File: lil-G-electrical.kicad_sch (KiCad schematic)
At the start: 34 parts, among them J101 XT-60, J102 XT-60, J103 GPIO, Q101 STD26P3LLH6, SW101 PVA1EE, U101 MCP1415, U102 TPS565208

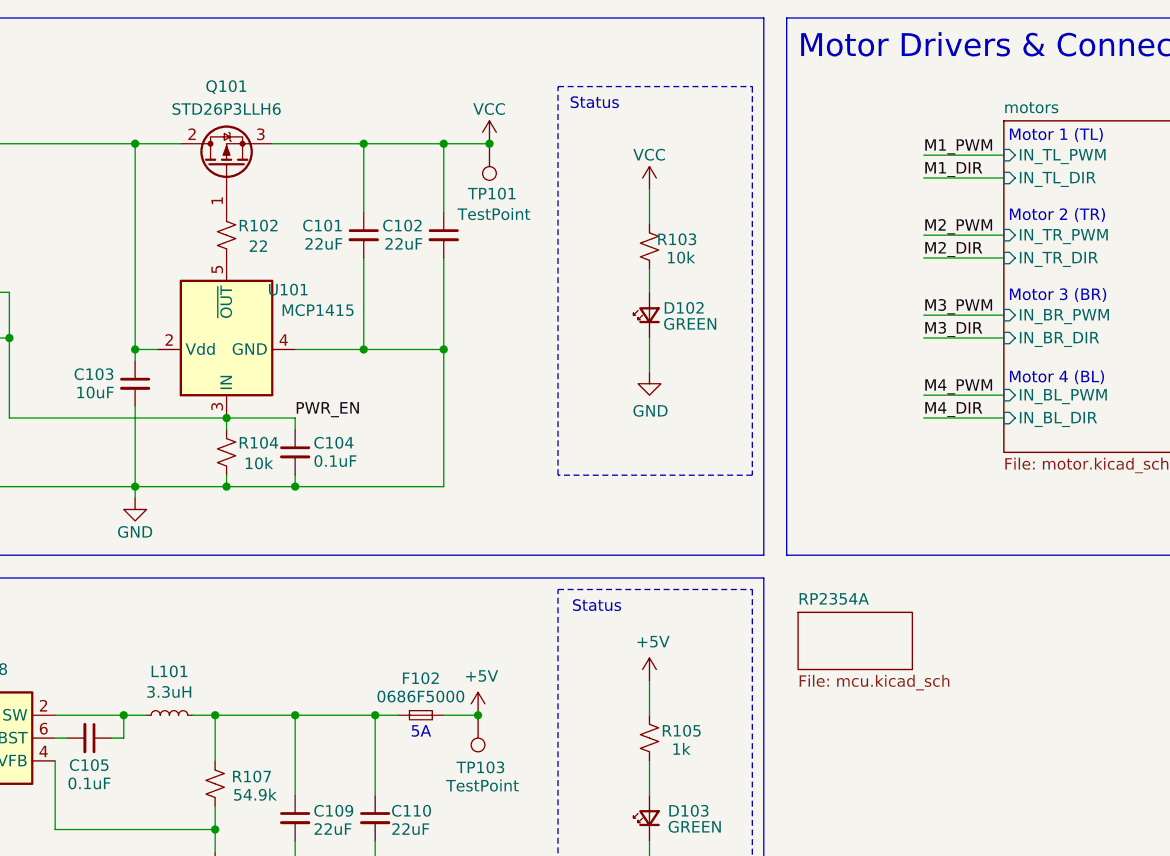
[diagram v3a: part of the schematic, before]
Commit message: fixed high-side power enable circuit. flipped PMOS source/drain
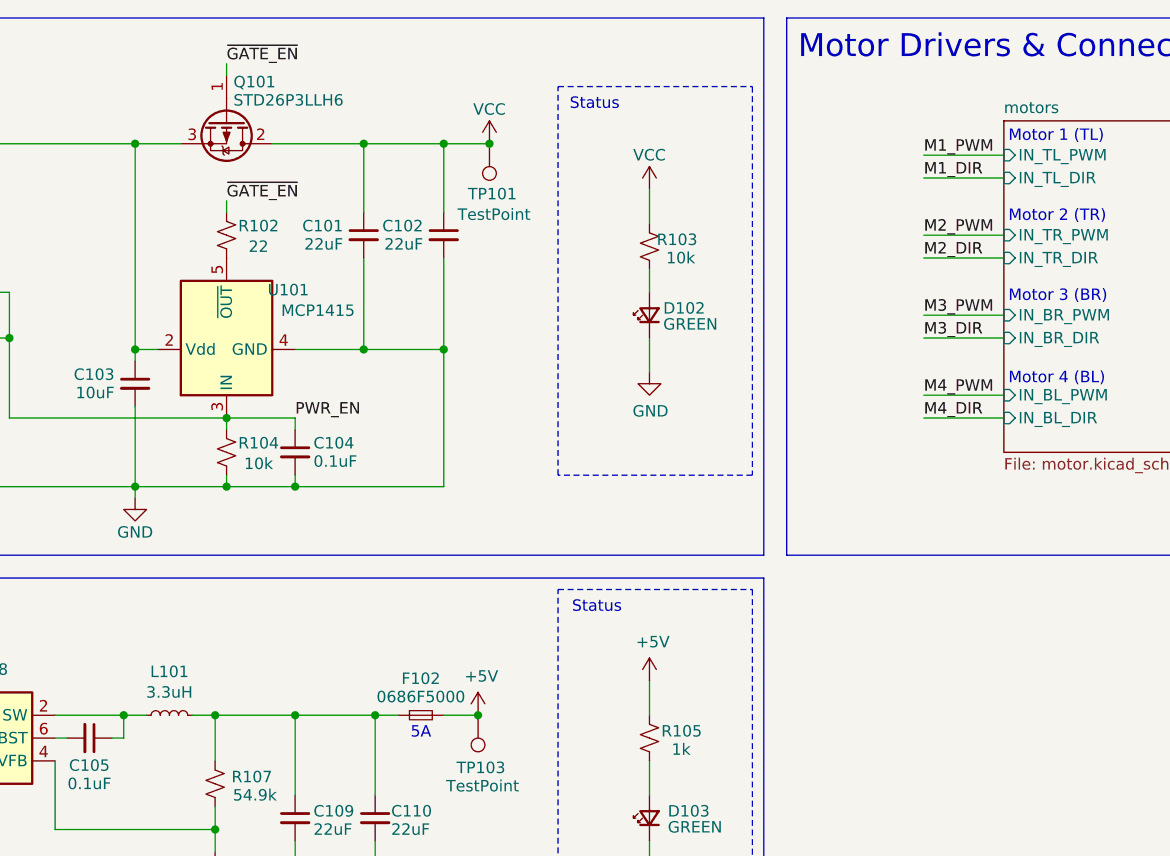
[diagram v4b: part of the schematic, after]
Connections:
- net VCC: now also Q101.2 (D); no longer Q101.3 (S)
- net at C103.1, F101.2, R101.1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: now also Q101.3 (S); no longer Q101.2 (D)
- net ~{GATE_EN}: now reaches Q101.1 (G), R102.1
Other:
- removed sheet RP2354A
- moved on the sheet: Q101
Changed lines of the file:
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@@
 	(wire
 		(pts
+			(xy 97.79 34.29) (xy 97.79 35.56)
+		)
+		(stroke
+			(width 0)
+			(type default)
+		)
+	)
+	(wire
+		(pts
 			(xy 68.58 144.78) (xy 93.98 144.78)
 		)
@@
 	(wire
 		(pts
+			(xy 97.79 19.05) (xy 97.79 20.32)
+		)
+		(stroke
+			(width 0)
+			(type default)
+		)
+	)
+	(wire
+		(pts
 			(xy 175.26 49.53) (xy 184.15 49.53)
 		)
@@
 		)
 	)
+	(label "~{GATE_EN}"
+		(at 97.79 19.05 0)
+		(fields_autoplaced yes)
+		(effects
+			(font
+				(size 1.27 1.27)
+			)
+			(justify left bottom)
+		)
+	)
 	(label "M4_DIR"
 		(at 175.26 58.42 0)
@@
 		)
 	)
+	(label "~{GATE_EN}"
+		(at 97.79 34.29 0)
+		(fields_autoplaced yes)
+		(effects
+			(font
+				(size 1.27 1.27)
+			)
+			(justify left bottom)
+		)
+	)
 	(label "M4_PWM"
 		(at 175.26 55.88 0)
@@
 	(symbol
 		(lib_id "Device:Q_PMOS_GDS")
-		(at 97.79 30.48 90)
+		(at 97.79 25.4 270)
 		(unit 1)
 		(exclude_from_sim no)
@@
 		(on_board yes)
 		(dnp no)
-		(fields_autoplaced yes)
 		(property "Reference" "Q101"
-			(at 97.79 21.59 90)
+			(at 98.552 21.082 90)
 			(effects
 				(font
 					(size 1.27 1.27)
 				)
+				(justify left)
 			)
 		)
 		(property "Value" "STD26P3LLH6"
-			(at 97.79 24.13 90)
+			(at 98.552 23.114 90)
 			(effects
 				(font
 					(size 1.27 1.27)
 				)
+				(justify left)
 			)
 		)
 		(property "Footprint" "Package_TO_SOT_SMD:TO-252-2"
-			(at 95.25 25.4 0)
+			(at 100.33 30.48 0)
 			(effects
 				(font
@@
 		)
 		(property "Datasheet" "~"
-			(at 97.79 30.48 0)
+			(at 97.79 25.4 0)
 			(effects
 				(font
@@
 		)
 		(property "Description" "P-MOSFET transistor, gate/drain/source"
-			(at 97.79 30.48 0)
+			(at 97.79 25.4 0)
 			(effects
 				(font
@@
 				)
 			)
-		)
-	)
-	(sheet
-		(at 161.29 80.01)
-		(size 12.7 6.35)
-		(fields_autoplaced yes)
-		(stroke
-			(width 0.1524)
-			(type solid)
-		)
-		(fill
-			(color 0 0 0 0.0000)
-		)
-		(property "Sheetname" "RP2354A"
-			(at 161.29 79.2984 0)
-			(effects
-				(font
-					(size 1.27 1.27)
-				)
-				(justify left bottom)
-			)
-		)
-		(property "Sheetfile" "mcu.kicad_sch"
-			(at 161.29 86.9446 0)
-			(effects
-				(font
-					(size 1.27 1.27)
-				)
-				(justify left top)
-			)
-		)
-		(instances
-			(project "lil-G-electrical"
-				(path "/e63e39d7-6ac0-4ffd-8aa3-1841a4541b55"
-					(page "3")
-				)
-			)

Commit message: version 2 done
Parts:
- removed D103: GREEN, LED_SMD:LED_0603_1608Metric, symbol Device:LED_Small
- removed J103: GPIO, Connector_PinSocket_2.54mm:PinSocket_2x20_P2.54mm_Vertical, symbol Connector_Generic:Conn_02x20_Odd_Even
- removed R105: 1k, Resistor_SMD:R_0603_1608Metric, symbol Device:R_Small_US
- removed SW101: PVA1EE, Button_Switch_THT:SW_Push_2P1T_Toggle_CK_PVA1xxH4xxxxxxV2, symbol Switch:SW_DPST
- removed TP102: TestPoint, TestPoint:TestPoint_Keystone_5000-5004_Miniature, symbol Connector:TestPoint
- added C11, C12: 10uF, Capacitor_SMD:C_0603_1608Metric, symbol Device:C_Small
- added C13: 100n, Capacitor_SMD:C_0402_1005Metric, symbol Device:C_Small
- added D3, D8: KT-0805G, LED_SMD:LED_0805_2012Metric, symbol Device:LED_Small
- added D4, D5, D6, D7: KT-0603W, LED_SMD:LED_0603_1608Metric, symbol Device:LED_Small
- added F3: 0467001.NRHF, Fuse:Fuse_0603_1608Metric, symbol Device:Fuse_Small
- added J2: XT30-U-M, Connector_AMASS:AMASS_XT30U-M_1x02_P5.0mm_Vertical, symbol Connector_Generic:Conn_01x02
- added J4: BM04B-SRSS-TB, Connector_JST:JST_SH_BM04B-SRSS-TB_1x04-1MP_P1.00mm_Vertical, symbol Connector_Generic_MountingPin:Conn_01x04_MountingPin
- added J5: BM03B-SRSS-TB, Connector_JST:JST_SH_BM03B-SRSS-TB_1x03-1MP_P1.00mm_Vertical, symbol Connector_Generic_MountingPin:Conn_01x03_MountingPin
- added R10, R11, R12, R13, R5, R9: 1k, Resistor_SMD:R_0402_1005Metric, symbol Device:R_Small_US
- added R14: 300k, Resistor_SMD:R_0603_1608Metric, symbol Device:R_Small_US
- added R15: 100k, Resistor_SMD:R_0603_1608Metric, symbol Device:R_Small_US
- added SW1: 5.8 ZSGT, lilG_footprints:5.8_ZSGT, symbol swwitches:SW_DPDT
- added TP2, TP4, TP5, TP6: 5001, TestPoint:TestPoint_Keystone_5000-5004_Miniature, symbol Connector:TestPoint
- added U3: NCP1117ST33T3G, digikey-footprints:SOT-223, symbol dk_PMIC-Voltage-Regulators-Linear:NCP1117ST33T3G
- C4: renamed from C104; value 0.1uF -> 100n; footprint Capacitor_SMD:C_0603_1608Metric -> Capacitor_SMD:C_0402_1005Metric
- C5: renamed from C105; value 0.1uF -> 100n; footprint Capacitor_SMD:C_0603_1608Metric -> Capacitor_SMD:C_0402_1005Metric
- C8: renamed from C108; value 0.1uF -> 100n; footprint Capacitor_SMD:C_0603_1608Metric -> Capacitor_SMD:C_0402_1005Metric
- D1: renamed from D102; value GREEN -> KT-0805G; footprint LED_SMD:LED_0603_1608Metric -> LED_SMD:LED_0805_2012Metric
- F1: renamed from F101; value 01000065Z -> 01530007Z; footprint lilG_footprints:LittleFuse_Mini_100_SMD -> lilG_footprints:LittleFuse_01530007Z
- F2: renamed from F102; value 0686F5000 -> S0603-S-5.0A
- J1: renamed from J101; value XT-60 -> XT60-PW-M; footprint Connector_AMASS:AMASS_XT60-M_1x02_P7.20mm_Vertical -> Connector_AMASS:AMASS_XT60PW-M_1x02_P7.20mm_Horizontal; now in the parts list
- J3: renamed from J102; value XT-60 -> XT60-PW-M; footprint Connector_AMASS:AMASS_XT60-M_1x02_P7.20mm_Vertical -> Connector_AMASS:AMASS_XT60PW-M_1x02_P7.20mm_Horizontal; now in the parts list
- L1: renamed from L101; value 3.3uH -> SRP5030T-3R3M
- Q1: renamed from Q101; value STD26P3LLH6 -> 40P30
- R1: renamed from R101; footprint Resistor_SMD:R_0603_1608Metric -> Resistor_SMD:R_0402_1005Metric
- R2: renamed from R103; value 10k -> 4.7k; footprint Resistor_SMD:R_0603_1608Metric -> Resistor_SMD:R_0402_1005Metric
- R3: renamed from R102; footprint Resistor_SMD:R_0603_1608Metric -> Resistor_SMD:R_0402_1005Metric
- R4: renamed from R104; footprint Resistor_SMD:R_0603_1608Metric -> Resistor_SMD:R_0402_1005Metric
- R6: renamed from R106; footprint Resistor_SMD:R_0603_1608Metric -> Resistor_SMD:R_0402_1005Metric
- R7: renamed from R107; footprint Resistor_SMD:R_0603_1608Metric -> Resistor_SMD:R_0402_1005Metric
- R8: renamed from R108; footprint Resistor_SMD:R_0603_1608Metric -> Resistor_SMD:R_0402_1005Metric
- TP1: renamed from TP101; value TestPoint -> 5001
- TP3: renamed from TP103; value TestPoint -> 5001
- renumbered C101 to C1, C110 to C10, C102 to C2, C103 to C3, C106 to C6, C107 to C7, C109 to C9, D101 to D2, U101 to U1, U102 to U2
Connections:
- net +3V3: now also F3.2, R10.2, R11.2, R12.2, R13.2, R9.1, TP6.1
- net +5V: now also J2.2 (Pin_2), R5.2
- net GND: now also C11.2, C12.2, C13.2, D3.1 (K), D8.1 (K), J2.1 (Pin_1), J4.MP (MountPin), J5.3 (Pin_3), J5.MP (MountPin), R15.1, TP2.1, U3.1 (ADJ/GND)
- net PWR_EN: now also SW1.1 (C), SW1.4 (C)
- net VCC: now also C11.1, R14.2, U3.3 (IN); no longer J3.2 (Pin_2)
- net VBAT_FUSED: now reaches C3.1, F1.2, Q1.3 (S), R1.1, U1.2 (Vdd)
- net BAT_1: now reaches D2.1 (K), F1.1, J1.2 (Pin_2)
- net BAT_1: now also J3.2 (Pin_2)
- net 5V_RAW: now reaches C10.1, C9.1, F2.1, L1.2, R7.2
- net at R1.2: now also SW1.2 (B), SW1.5 (B)
- new net: D6.2 (A), R11.1
- new net: C12.1, F3.1, U3.2 (OUT), U3.4 (OUT)
- new net: D7.2 (A), R12.1
- new net: D3.2 (A), R5.1
- new net: D5.2 (A), R10.1
- new net: D4.2 (A), R9.2
- new net: D8.2 (A), R13.1
- new net DBG_1: D4.1 (K)
- new net DBG_2: D5.1 (K)
- new net DBG_3: D6.1 (K)
- new net DBG_4: D7.1 (K)
- new net I2C_SCL: J5.2 (Pin_2), TP4.1
- new net I2C_SDA: J5.1 (Pin_1), TP5.1
- new net SPI_CSn: J4.2 (Pin_2)
- new net SPI_RX: J4.1 (Pin_1)
- new net SPI_SCK: J4.3 (Pin_3)
- new net SPI_TX: J4.4 (Pin_4)
- new net VBAT_READ: C13.1, R14.1, R15.2
- no-connect marks 0 -> 3
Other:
- sheet motors renamed motor 1
- added sheet bmi160 (imu.kicad_sch)
- added sheet motor 2 (motor.kicad_sch)
- added sheet motor 3 (motor.kicad_sch)
- added sheet motor 4 (motor.kicad_sch)
- added sheet rp2350a (control.kicad_sch)
- sheet motor 1 ports: added ENC_A, ENC_B, PWM_A, PWM_B; removed IN_BL_DIR, IN_BL_PWM, IN_BR_DIR, IN_BR_PWM, IN_TL_DIR, IN_TL_PWM, IN_TR_DIR, IN_TR_PWM, M1_ENC_A, M1_ENC_B, M2_ENC_A, M2_ENC_B, M3_ENC_A, M3_ENC_B, M4_ENC_A, M4_ENC_B
- note added: "100% ~ 3.15V"
- note added: "1A"
- note added: "3.3u"
- note added: "3V3 1A LDO"
- note added: "5V 5A Buck"
- note added: "Backup"
- note added: "Battery Voltage"
- note added: "DBG"
- note added: "Data (I2C Connector)"
- note added: "Data (SPI Connector)"
- note added: "Divider factor = 1/4"
- note added: "IMU"
- note added: "MCU"
- note added: "Power"
- note added: "RPI5 Connectors"
- note removed: "5V 5A Regulator"
- note removed: "Emergency Direct VCC"
- note removed: "GPIO10/SPI0.MOSI"
- note removed: "GPIO11/SPI0.SCLK"
- note removed: "GPIO12/PWM0"
- note removed: "GPIO13/PWM1"
- note removed: "GPIO14/TXD0"
- note removed: "GPIO15/RXD0"
- note removed: "GPIO16"
- note removed: "GPIO17"
- note removed: "GPIO18/PCM.CLK"
- note removed: "GPIO19/PCM.FS"
- note removed: "GPIO2/SDA1"
- note removed: "GPIO20/PCM.DIN"
- note removed: "GPIO21/PCM.DOUT"
- note removed: "GPIO22"
- note removed: "GPIO23"
- note removed: "GPIO24"
- note removed: "GPIO25"
- note removed: "GPIO26"
- note removed: "GPIO27"
- note removed: "GPIO3/SCL1"
- note removed: "GPIO4/GPCLK0"
- note removed: "GPIO5"
- note removed: "GPIO6"
- note removed: "GPIO7/SPI0.CE1"
- note removed: "GPIO8/SPI0.CE0"
- note removed: "GPIO9/SPI0.MISO"
- note removed: "ID_SCL"
- note removed: "ID_SDA"
- note removed: "Motor 1 (TL)"
- note removed: "Motor 2 (TR)"
- note removed: "Motor 3 (BR)"
- note removed: "Motor 4 (BL)"
- note removed: "RPI 5 Header"
- moved on the sheet: D1, D2, F1, J1, J3, Q1, R1, R2, TP1, TP3

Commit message: last modification for v2.0 before submitting order
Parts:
- added TP6, TP8, TP9: 5001, TestPoint:TestPoint_Keystone_5000-5004_Miniature, symbol Connector:TestPoint
- renumbered R14 to R10, R9 to R11, R10 to R12, R11 to R13, R12 to R14, R13 to R9, TP3 to TP2, TP5 to TP3, TP6 to TP5, TP2 to TP7
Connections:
- net GND: now also TP6.1, TP8.1, TP9.1
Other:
- sheet bmi160 renamed LSMDSOX
- moved on the sheet: TP7
